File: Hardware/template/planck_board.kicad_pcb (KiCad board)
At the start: 2 copper layers, 80.8 x 60.1 mm, 6 parts, among them J1 Conn_01x40

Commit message: update pin names
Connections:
- net EX4 renamed ~INH~
- net EX5 renamed ~SLOT_SEL~
- net EX6 renamed LED1
- net EX7 renamed LED2
- net EX8 renamed LED3
- net EX9 renamed LED4
- net IRQ renamed ~IRQ~
- net IRQ0 renamed ~SLOT_IRQ~
- net IRQ3 renamed CLK_12M
- net NMI renamed ~NMI~
- net RESET renamed ~RESET~
- net RW renamed R~W~
- J1 pad 22: EX2 -> ~SLOW~
- J1 pad 28: EX3 -> ~SSEL~
- J1 pad 44: IRQ2 -> EX2
- J1 pad 46: IRQ1 -> EX3
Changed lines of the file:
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@@
   )
   (net 0 "")
-  (net 1 NMI)
-  (net 2 RESET)
-  (net 3 RDY)
-  (net 4 A15)
-  (net 5 A14)
-  (net 6 A13)
-  (net 7 A12)
-  (net 8 A11)
-  (net 9 GND)
-  (net 10 +5V)
-  (net 11 A10)
-  (net 12 A9)
-  (net 13 A8)
-  (net 14 D7)
-  (net 15 A7)
-  (net 16 D6)
-  (net 17 A6)
-  (net 18 D5)
-  (net 19 A5)
-  (net 20 D4)
-  (net 21 A4)
-  (net 22 D3)
-  (net 23 A3)
-  (net 24 D2)
-  (net 25 A2)
-  (net 26 D1)
-  (net 27 A1)
-  (net 28 D0)
-  (net 29 A0)
-  (net 30 IRQ0)
-  (net 31 RW)
-  (net 32 IRQ1)
-  (net 33 IRQ)
-  (net 34 IRQ2)
-  (net 35 IRQ3)
-  (net 36 CLK)
-  (net 37 BE)
-  (net 38 SYNC)
-  (net 39 EX9)
-  (net 40 EX8)
-  (net 41 EX7)
-  (net 42 EX6)
-  (net 43 EX5)
-  (net 44 EX4)
-  (net 45 EX3)
-  (net 46 EX2)
-  (net 47 EX1)
-  (net 48 EX0)
+  (net 1 RDY)
+  (net 2 A15)
+  (net 3 A14)
+  (net 4 A13)
+  (net 5 A12)
+  (net 6 A11)
+  (net 7 GND)
+  (net 8 +5V)
+  (net 9 A10)
+  (net 10 A9)
+  (net 11 A8)
+  (net 12 D7)
+  (net 13 A7)
+  (net 14 D6)
+  (net 15 A6)
+  (net 16 D5)
+  (net 17 A5)
+  (net 18 D4)
+  (net 19 A4)
+  (net 20 D3)
+  (net 21 A3)
+  (net 22 D2)
+  (net 23 A2)
+  (net 24 D1)
+  (net 25 A1)
+  (net 26 D0)
+  (net 27 A0)
+  (net 28 CLK)
+  (net 29 BE)
+  (net 30 SYNC)
+  (net 31 EX3)
+  (net 32 EX2)
+  (net 33 EX1)
+  (net 34 EX0)
+  (net 35 ~NMI~)
+  (net 36 ~RESET~)
+  (net 37 ~SLOT_IRQ~)
+  (net 38 ~IRQ~)
+  (net 39 R~W~)
+  (net 40 CLK_12M)
+  (net 41 LED4)
+  (net 42 LED3)
+  (net 43 LED2)
+  (net 44 LED1)
+  (net 45 ~SLOT_SEL~)
+  (net 46 ~INH~)
+  (net 47 ~SSEL~)
+  (net 48 ~SLOW~)
   (net_class Default "This is the default net class."
     (clearance 0.2)
@@
     (add_net BE)
     (add_net CLK)
+    (add_net CLK_12M)
     (add_net D0)
     (add_net D1)
@@
     (add_net EX2)
     (add_net EX3)
-    (add_net EX4)
-    (add_net EX5)
-    (add_net EX6)
-    (add_net EX7)
-    (add_net EX8)
-    (add_net EX9)
     (add_net GND)
-    (add_net IRQ)
-    (add_net IRQ0)
-    (add_net IRQ1)
-    (add_net IRQ2)
-    (add_net IRQ3)
-    (add_net NMI)
+    (add_net LED1)
+    (add_net LED2)
+    (add_net LED3)
+    (add_net LED4)
     (add_net RDY)
-    (add_net RESET)
-    (add_net RW)
+    (add_net R~W~)
     (add_net SYNC)
+    (add_net ~INH~)
+    (add_net ~IRQ~)
+    (add_net ~NMI~)
+    (add_net ~RESET~)
+    (add_net ~SLOT_IRQ~)
+    (add_net ~SLOT_SEL~)
+    (add_net ~SLOW~)
+    (add_net ~SSEL~)
   )
   (module logo:logo (layer B.Cu)
@@
     )
     (pad 50 thru_hole oval (at 2.54 60.96 270) (size 1.7 1.7) (drill 1) (layers *.Cu *.Mask)
-      (net 1 NMI))
+      (net 35 ~NMI~))
     (pad 49 thru_hole oval (at 0 60.96 270) (size 1.7 1.7) (drill 1) (layers *.Cu *.Mask)
-      (net 2 RESET))
+      (net 36 ~RESET~))
     (pad 48 thru_hole oval (at 2.54 58.42 270) (size 1.7 1.7) (drill 1) (layers *.Cu *.Mask)
-      (net 30 IRQ0))
+      (net 37 ~SLOT_IRQ~))
     (pad 47 thru_hole oval (at 0 58.42 270) (size 1.7 1.7) (drill 1) (layers *.Cu *.Mask)
-      (net 38 SYNC))
+      (net 30 SYNC))
     (pad 46 thru_hole oval (at 2.54 55.88 270) (size 1.7 1.7) (drill 1) (layers *.Cu *.Mask)
-      (net 32 IRQ1))
+      (net 31 EX3))
     (pad 45 thru_hole oval (at 0 55.88 270) (size 1.7 1.7) (drill 1) (layers *.Cu *.Mask)
-      (net 33 IRQ))
+      (net 38 ~IRQ~))
     (pad 44 thru_hole oval (at 2.54 53.34 270) (size 1.7 1.7) (drill 1) (layers *.Cu *.Mask)
-      (net 34 IRQ2))
+      (net 32 EX2))
     (pad 43 thru_hole oval (at 0 53.34 270) (size 1.7 1.7) (drill 1) (layers *.Cu *.Mask)
-      (net 31 RW))
+      (net 39 R~W~))
     (pad 42 thru_hole oval (at 2.54 50.8 270) (size 1.7 1.7) (drill 1) (layers *.Cu *.Mask)
-      (net 35 IRQ3))
+      (net 40 CLK_12M))
     (pad 41 thru_hole oval (at 0 50.8 270) (size 1.7 1.7) (drill 1) (layers *.Cu *.Mask)
-      (net 36 CLK))
+      (net 28 CLK))
     (pad 40 thru_hole oval (at 2.54 48.26 270) (size 1.7 1.7) (drill 1) (layers *.Cu *.Mask)
-      (net 39 EX9))
+      (net 41 LED4))
     (pad 39 thru_hole oval (at 0 48.26 270) (size 1.7 1.7) (drill 1) (layers *.Cu *.Mask)
-      (net 37 BE))
+      (net 29 BE))
     (pad 38 thru_hole oval (at 2.54 45.72 270) (size 1.7 1.7) (drill 1) (layers *.Cu *.Mask)
-      (net 40 EX8))
+      (net 42 LED3))
     (pad 37 thru_hole oval (at 0 45.72 270) (size 1.7 1.7) (drill 1) (layers *.Cu *.Mask)
-      (net 3 RDY))
+      (net 1 RDY))
     (pad 36 thru_hole oval (at 2.54 43.18 270) (size 1.7 1.7) (drill 1) (layers *.Cu *.Mask)
-      (net 41 EX7))
+      (net 43 LED2))
     (pad 35 thru_hole oval (at 0 43.18 270) (size 1.7 1.7) (drill 1) (layers *.Cu *.Mask)
-      (net 4 A15))
+      (net 2 A15))
     (pad 34 thru_hole oval (at 2.54 40.64 270) (size 1.7 1.7) (drill 1) (layers *.Cu *.Mask)
-      (net 42 EX6))
+      (net 44 LED1))
     (pad 33 thru_hole oval (at 0 40.64 270) (size 1.7 1.7) (drill 1) (layers *.Cu *.Mask)
-      (net 5 A14))
+      (net 3 A14))
     (pad 32 thru_hole oval (at 2.54 38.1 270) (size 1.7 1.7) (drill 1) (layers *.Cu *.Mask)
-      (net 43 EX5))
+      (net 45 ~SLOT_SEL~))
     (pad 31 thru_hole oval (at 0 38.1 270) (size 1.7 1.7) (drill 1) (layers *.Cu *.Mask)
-      (net 6 A13))
+      (net 4 A13))
     (pad 30 thru_hole oval (at 2.54 35.56 270) (size 1.7 1.7) (drill 1) (layers *.Cu *.Mask)
-      (net 44 EX4))
+      (net 46 ~INH~))
     (pad 29 thru_hole oval (at 0 35.56 270) (size 1.7 1.7) (drill 1) (layers *.Cu *.Mask)
-      (net 7 A12))
+      (net 5 A12))
     (pad 28 thru_hole oval (at 2.54 33.02 270) (size 1.7 1.7) (drill 1) (layers *.Cu *.Mask)
-      (net 45 EX3))
+      (net 47 ~SSEL~))
     (pad 27 thru_hole oval (at 0 33.02 270) (size 1.7 1.7) (drill 1) (layers *.Cu *.Mask)
-      (net 8 A11))
+      (net 6 A11))
     (pad 26 thru_hole oval (at 2.54 30.48 270) (size 1.7 1.7) (drill 1) (layers *.Cu *.Mask)
-      (net 9 GND))
+      (net 7 GND))
     (pad 25 thru_hole oval (at 0 30.48 270) (size 1.7 1.7) (drill 1) (layers *.Cu *.Mask)
-      (net 10 +5V))
+      (net 8 +5V))
     (pad 24 thru_hole oval (at 2.54 27.94 270) (size 1.7 1.7) (drill 1) (layers *.Cu *.Mask)
-      (net 10 +5V))
+      (net 8 +5V))
     (pad 23 thru_hole oval (at 0 27.94 270) (size 1.7 1.7) (drill 1) (layers *.Cu *.Mask)
-      (net 9 GND))
+      (net 7 GND))
     (pad 22 thru_hole oval (at 2.54 25.4 270) (size 1.7 1.7) (drill 1) (layers *.Cu *.Mask)
-      (net 46 EX2))
+      (net 48 ~SLOW~))
     (pad 21 thru_hole oval (at 0 25.4 270) (size 1.7 1.7) (drill 1) (layers *.Cu *.Mask)
-      (net 11 A10))
+      (net 9 A10))
     (pad 20 thru_hole oval (at 2.54 22.86 270) (size 1.7 1.7) (drill 1) (layers *.Cu *.Mask)
-      (net 47 EX1))
+      (net 33 EX1))
     (pad 19 thru_hole oval (at 0 22.86 270) (size 1.7 1.7) (drill 1) (layers *.Cu *.Mask)
-      (net 12 A9))
+      (net 10 A9))
     (pad 18 thru_hole oval (at 2.54 20.32 270) (size 1.7 1.7) (drill 1) (layers *.Cu *.Mask)
-      (net 48 EX0))
+      (net 34 EX0))
     (pad 17 thru_hole oval (at 0 20.32 270) (size 1.7 1.7) (drill 1) (layers *.Cu *.Mask)
-      (net 13 A8))
+      (net 11 A8))
     (pad 16 thru_hole oval (at 2.54 17.78 270) (size 1.7 1.7) (drill 1) (layers *.Cu *.Mask)
-      (net 14 D7))
+      (net 12 D7))
     (pad 15 thru_hole oval (at 0 17.78 270) (size 1.7 1.7) (drill 1) (layers *.Cu *.Mask)
-      (net 15 A7))
+      (net 13 A7))
     (pad 14 thru_hole oval (at 2.54 15.24 270) (size 1.7 1.7) (drill 1) (layers *.Cu *.Mask)
-      (net 16 D6))
+      (net 14 D6))
     (pad 13 thru_hole oval (at 0 15.24 270) (size 1.7 1.7) (drill 1) (layers *.Cu *.Mask)
-      (net 17 A6))
+      (net 15 A6))
     (pad 12 thru_hole oval (at 2.54 12.7 270) (size 1.7 1.7) (drill 1) (layers *.Cu *.Mask)
-      (net 18 D5))
+      (net 16 D5))
     (pad 11 thru_hole oval (at 0 12.7 270) (size 1.7 1.7) (drill 1) (layers *.Cu *.Mask)
-      (net 19 A5))
+      (net 17 A5))
     (pad 10 thru_hole oval (at 2.54 10.16 270) (size 1.7 1.7) (drill 1) (layers *.Cu *.Mask)
-      (net 20 D4))
+      (net 18 D4))
     (pad 9 thru_hole oval (at 0 10.16 270) (size 1.7 1.7) (drill 1) (layers *.Cu *.Mask)
-      (net 21 A4))
+      (net 19 A4))
     (pad 8 thru_hole oval (at 2.54 7.62 270) (size 1.7 1.7) (drill 1) (layers *.Cu *.Mask)
-      (net 22 D3))
+      (net 20 D3))
     (pad 7 thru_hole oval (at 0 7.62 270) (size 1.7 1.7) (drill 1) (layers *.Cu *.Mask)
-      (net 23 A3))
+      (net 21 A3))
     (pad 6 thru_hole oval (at 2.54 5.08 270) (size 1.7 1.7) (drill 1) (layers *.Cu *.Mask)
-      (net 24 D2))
+      (net 22 D2))
     (pad 5 thru_hole oval (at 0 5.08 270) (size 1.7 1.7) (drill 1) (layers *.Cu *.Mask)
-      (net 25 A2))
+      (net 23 A2))
     (pad 4 thru_hole oval (at 2.54 2.54 270) (size 1.7 1.7) (drill 1) (layers *.Cu *.Mask)
-      (net 26 D1))
+      (net 24 D1))
     (pad 3 thru_hole oval (at 0 2.54 270) (size 1.7 1.7) (drill 1) (layers *.Cu *.Mask)
-      (net 27 A1))
+      (net 25 A1))
     (pad 2 thru_hole oval (at 2.54 0 270) (size 1.7 1.7) (drill 1) (layers *.Cu *.Mask)
-      (net 28 D0))
+      (net 26 D0))
     (pad 1 thru_hole rect (at 0 0 270) (size 1.7 1.7) (drill 1) (layers *.Cu *.Mask)
-      (net 29 A0))
+      (net 27 A0))
     (model ${KISYS3DMOD}/Connector_PinHeader_2.54mm.3dshapes/PinHeader_2x25_P2.54mm_Horizontal.wrl
       (at (xyz 0 0 0))
@@
   (gr_line (start 80.772 0) (end 13.97 0) (layer Edge.Cuts) (width 0.1))
   (gr_line (start 80.772 -57.912) (end 80.772 0) (layer Edge.Cuts) (width 0.1))
-  (zone (net 10) (net_name +5V) (layer F.Cu) (hatch edge 0.508)
+  (zone (net 8) (net_name +5V) (layer F.Cu) (hatch edge 0.508)
     (connect_pads (clearance 0.508))
     (min_thickness 0.254)
@@
     )
   )
-  (zone (net 9) (net_name GND) (layer B.Cu) (hatch edge 0.508)
+  (zone (net 7) (net_name GND) (layer B.Cu) (hatch edge 0.508)
     (connect_pads (clearance 0.508))
     (min_thickness 0.254)

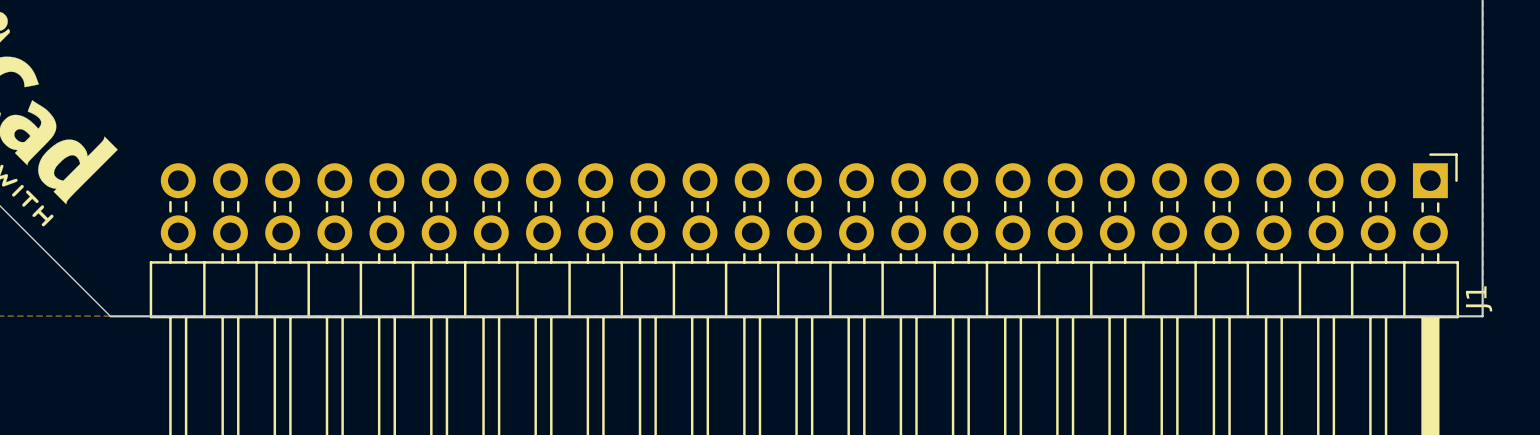
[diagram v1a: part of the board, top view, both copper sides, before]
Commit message: update with pin numbers on silkscreen
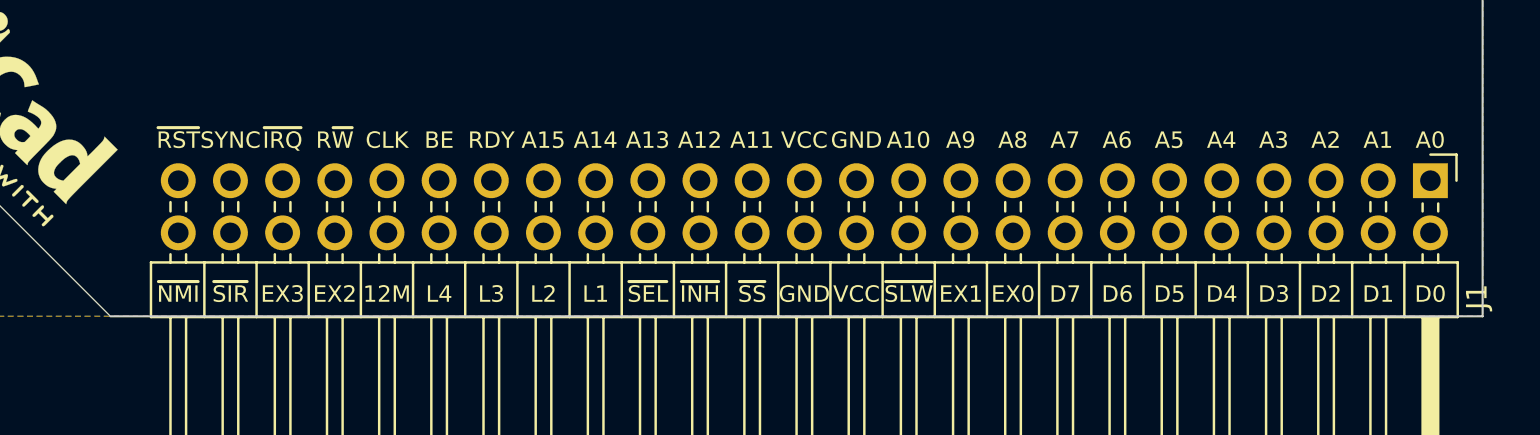
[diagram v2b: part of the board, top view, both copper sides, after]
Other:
- board text added: "12M"
- board text added: "A0"
- board text added: "A1"
- board text added: "A10"
- board text added: "A11"
- board text added: "A12"
- board text added: "A13"
- board text added: "A14"
- board text added: "A15"
- board text added: "A2"
- board text added: "A3"
- board text added: "A4"
- board text added: "A5"
- board text added: "A6"
- board text added: "A7"
- board text added: "A8"
- board text added: "A9"
- board text added: "BE"
- board text added: "CLK"
- board text added: "D0"
- board text added: "D1"
- board text added: "D2"
- board text added: "D3"
- board text added: "D4"
- board text added: "D5"
- board text added: "D6"
- board text added: "D7"
- board text added: "EX0"
- board text added: "EX1"
- board text added: "EX2"
- board text added: "EX3"
- board text added: "GND"
- board text added: "L1"
- board text added: "L2"
- board text added: "L3"
- board text added: "L4"
- board text added: "RDY"
- board text added: "R~W~"
- board text added: "SYNC"
- board text added: "VCC"
- board text added: "~INH~"
- board text added: "~IRQ~"
- board text added: "~NMI~"
- board text added: "~RST~"
- board text added: "~SEL~"
- board text added: "~SIR~"
- board text added: "~SLW~"
- board text added: "~SS~"

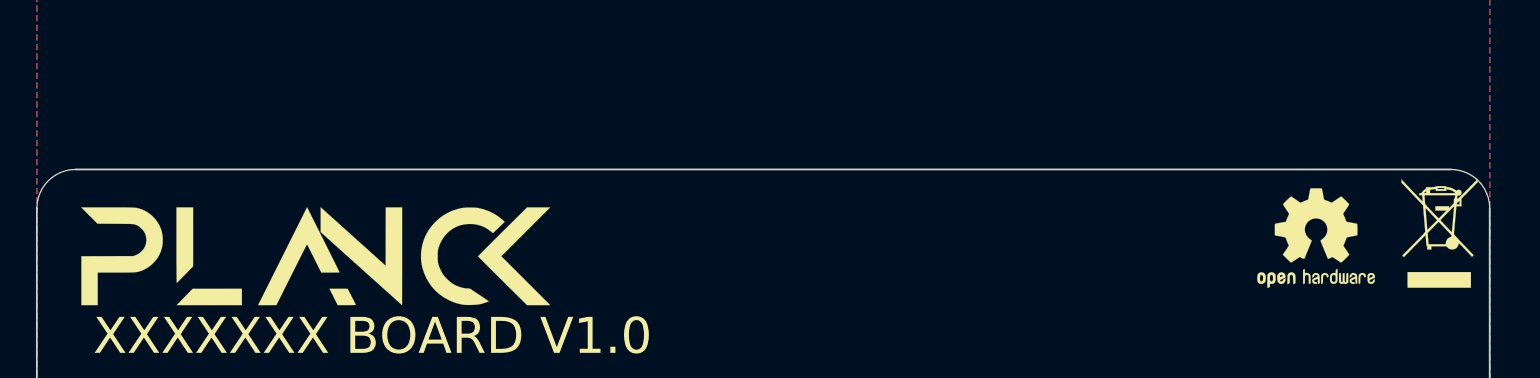
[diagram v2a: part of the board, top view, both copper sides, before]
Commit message: Add Pico VGA board + update midi board
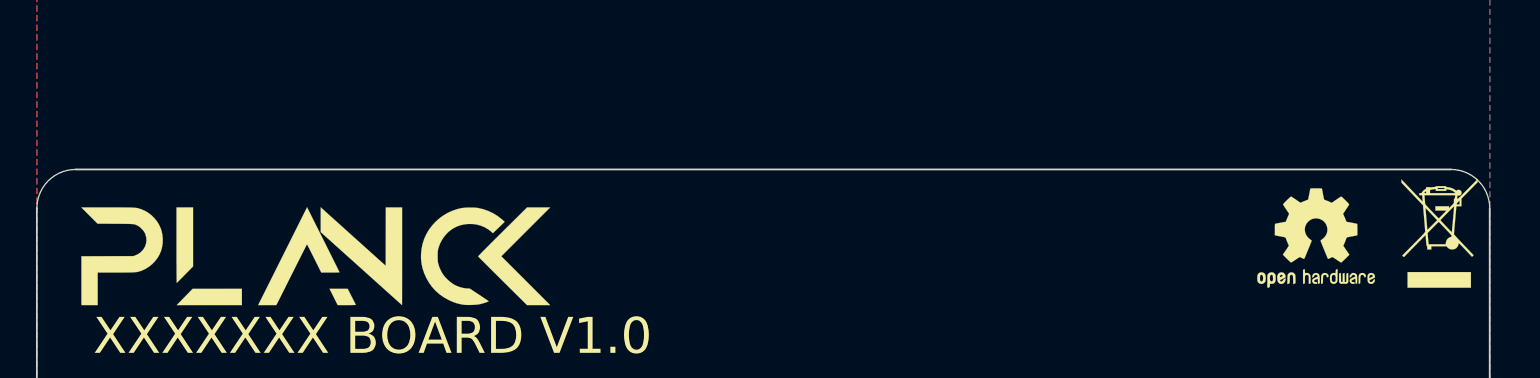
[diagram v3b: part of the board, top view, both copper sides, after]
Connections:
- net R~W~ renamed R~{W}
- net ~INH~ renamed ~{INH}
- net ~IRQ~ renamed ~{IRQ}
- net ~NMI~ renamed ~{NMI}
- net ~RESET~ renamed ~{RESET}
- net ~SLOT_IRQ~ renamed ~{SLOT_IRQ}
- net ~SLOT_SEL~ renamed ~{SLOT_SEL}
- net ~SLOW~ renamed ~{SLOW}
- net ~SSEL~ renamed ~{SSEL}
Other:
- net class Default removed
- board text added: "R~{W}"
- board text added: "~{INH}"
- board text added: "~{IRQ}"
- board text added: "~{NMI}"
- board text added: "~{RST}"
- board text added: "~{SEL}"
- board text added: "~{SIR}"
- board text added: "~{SLW}"
- board text added: "~{SS}"
- board text removed: "R~W~"
- board text removed: "~INH~"
- board text removed: "~IRQ~"
- board text removed: "~NMI~"
- board text removed: "~RST~"
- board text removed: "~SEL~"
- board text removed: "~SIR~"
- board text removed: "~SLW~"
- board text removed: "~SS~"
